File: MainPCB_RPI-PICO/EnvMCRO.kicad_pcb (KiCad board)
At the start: 2 copper layers, 109.6 x 69.7 mm, 43 parts, among them SW1 Rotary_Encoder_Switch, U1 Pico

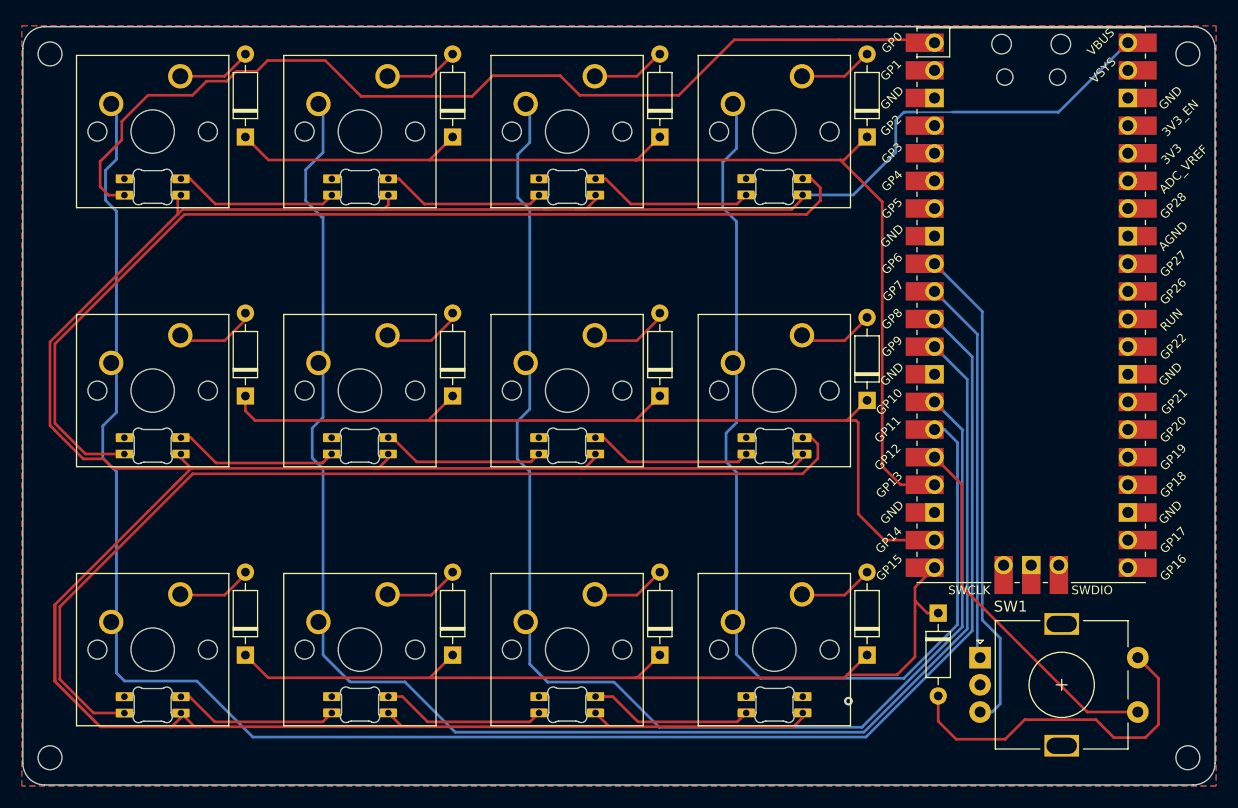
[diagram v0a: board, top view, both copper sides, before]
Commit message: updated macro boards to have padded mount holes and github url
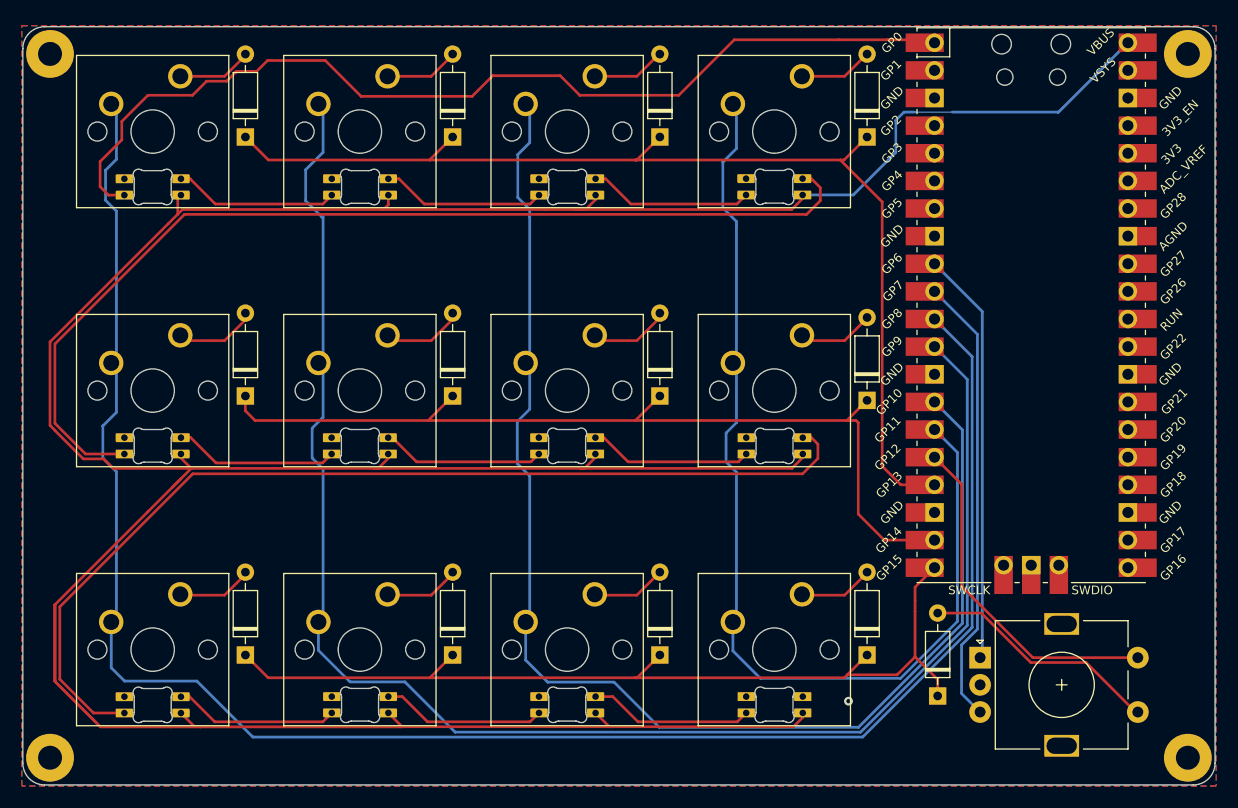
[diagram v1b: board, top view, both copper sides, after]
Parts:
- H1, H2, H3, H4: footprint MountingHole:MountingHole_2.2mm_M2 -> MountingHole:MountingHole_2.2mm_M2_Pad
- moved D_14 7.62 mm to (147.5, 100.3), turned to 90 degrees
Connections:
- SW1 pad A: ROTA -> ROTB
- SW1 pad B: ROTB -> ROTA
- SW1 pad S1: col4 -> Net-(D_14-Pad2)
- SW1 pad S2: Net-(D_14-Pad2) -> col4
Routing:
- net Net-(D_14-Pad2): track 32.1 -> 22.2 mm
- net ROTB: track 45.1 -> 38.5 mm
- net ROTA: track 35.4 -> 41.6 mm
- net col4: track 33.9 -> 31.8 mm
- net row2: track 83.4 -> 85.3 mm
- net VBUS: track 331.1 -> 329.5 mm
- net col3: track 95.9 -> 95.2 mm
- net GND: track 0.00 -> 0.63 mm
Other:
- board text added: "https://github.com/Envious-Data/Env-MCRO"

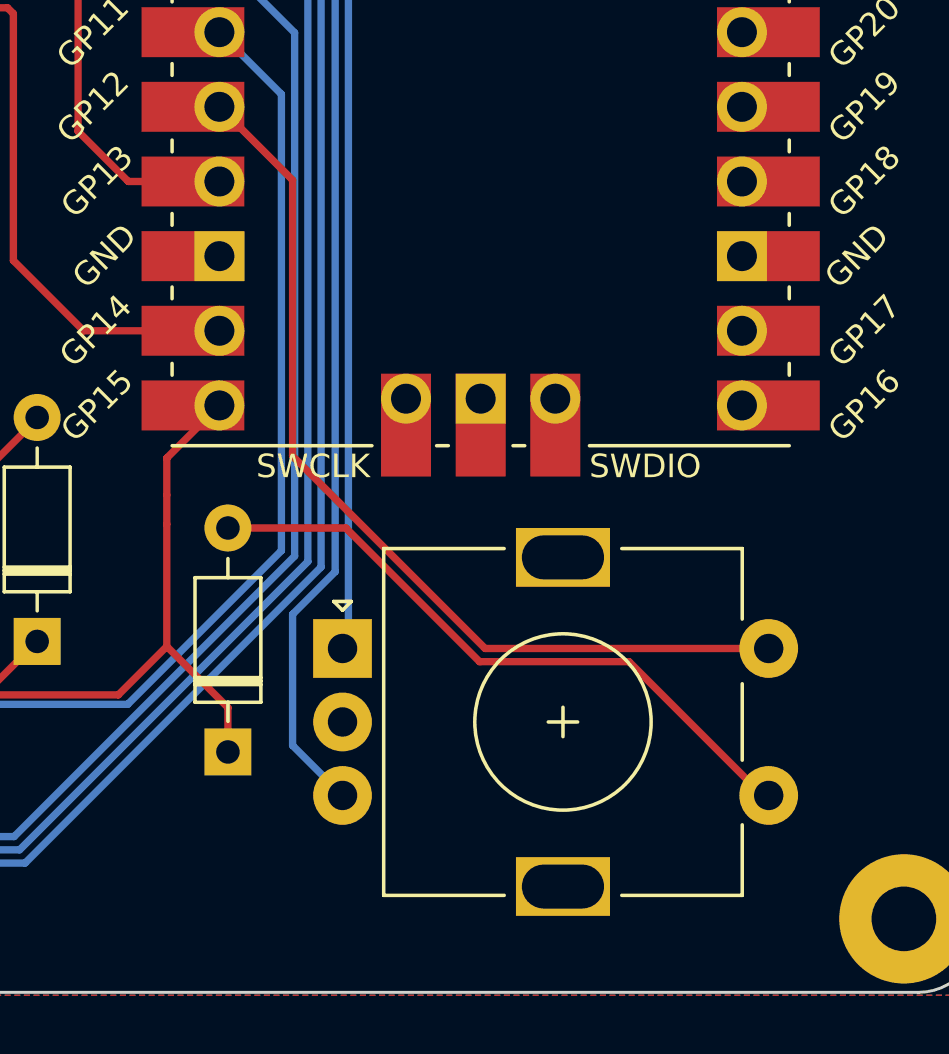
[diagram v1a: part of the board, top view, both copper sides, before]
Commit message: swapped EC11 for EC12 because cheaper, might swap again to what ever people get a hold of the easiest.
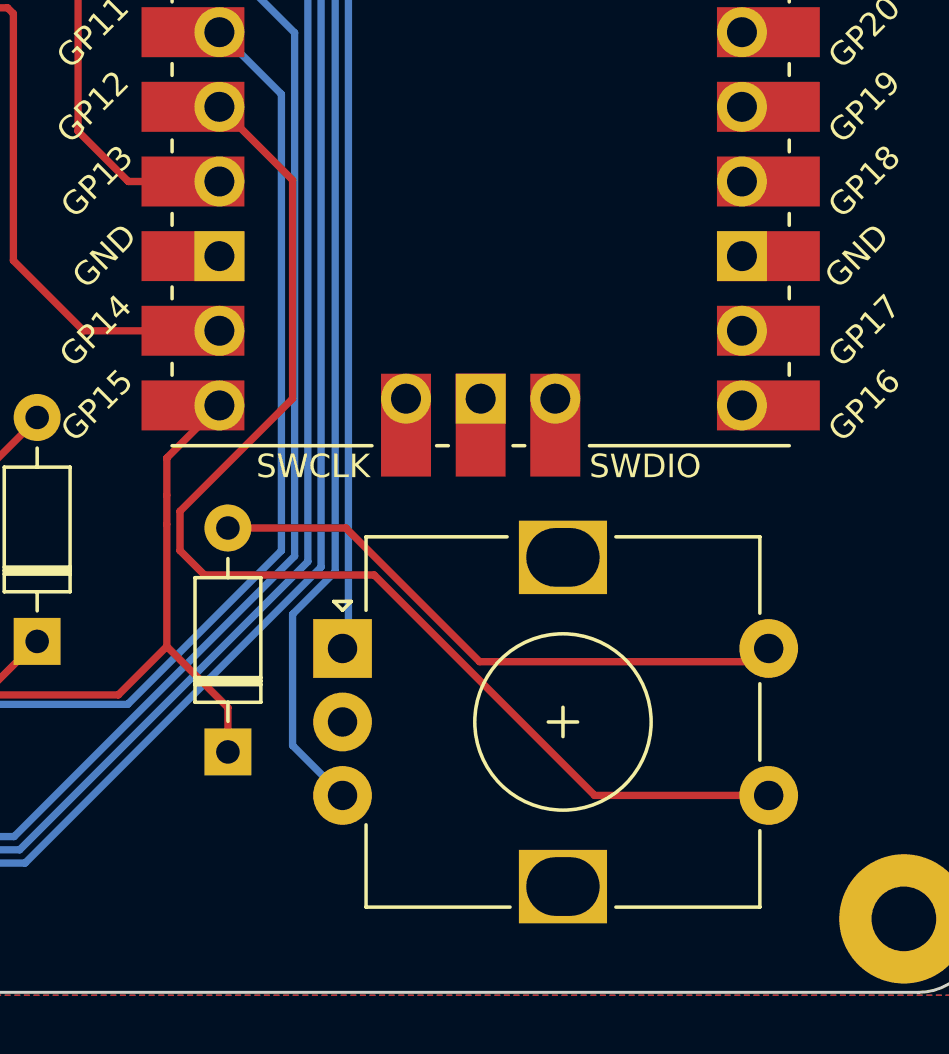
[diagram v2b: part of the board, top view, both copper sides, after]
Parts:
- SW1: footprint Rotary_Encoder:RotaryEncoder_Alps_EC11E-Switch_Vertical_H20mm -> Rotary_Encoder:RotaryEncoder_Alps_EC12E-Switch_Vertical_H20mm
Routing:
- net col4: track 31.8 -> 41.4 mm
- net Net-(D_14-Pad2): track 22.2 -> 20.5 mm

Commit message: fixed pads and generated updated gerber
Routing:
- net Net-(D4-Pad2): track 93.8 -> 96.9 mm
- net VBUS: vias 0 -> 1
- net GND: vias 1 -> 10
